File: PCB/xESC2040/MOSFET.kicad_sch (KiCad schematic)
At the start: 6 parts, among them J6 Conn_02x02_Counter_Clockwise, Q1 BSC026N08NS5, Q2 BSC026N08NS5

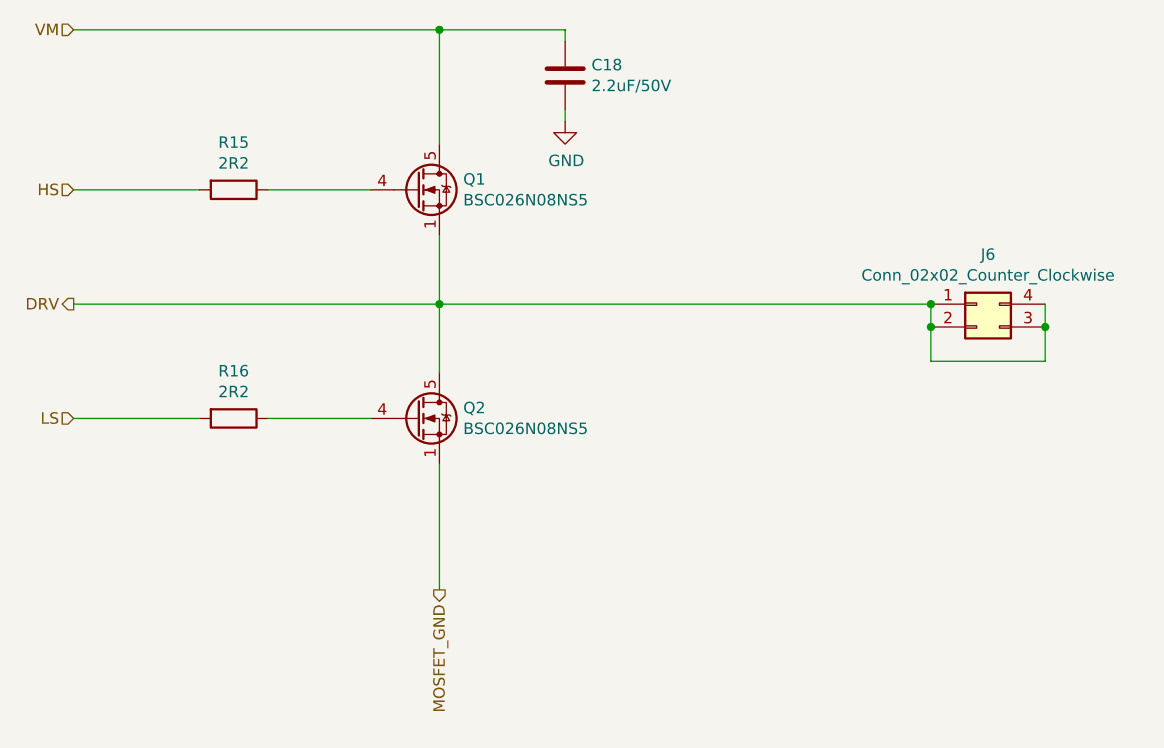
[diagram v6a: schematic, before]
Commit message: updated wrong BOM part number
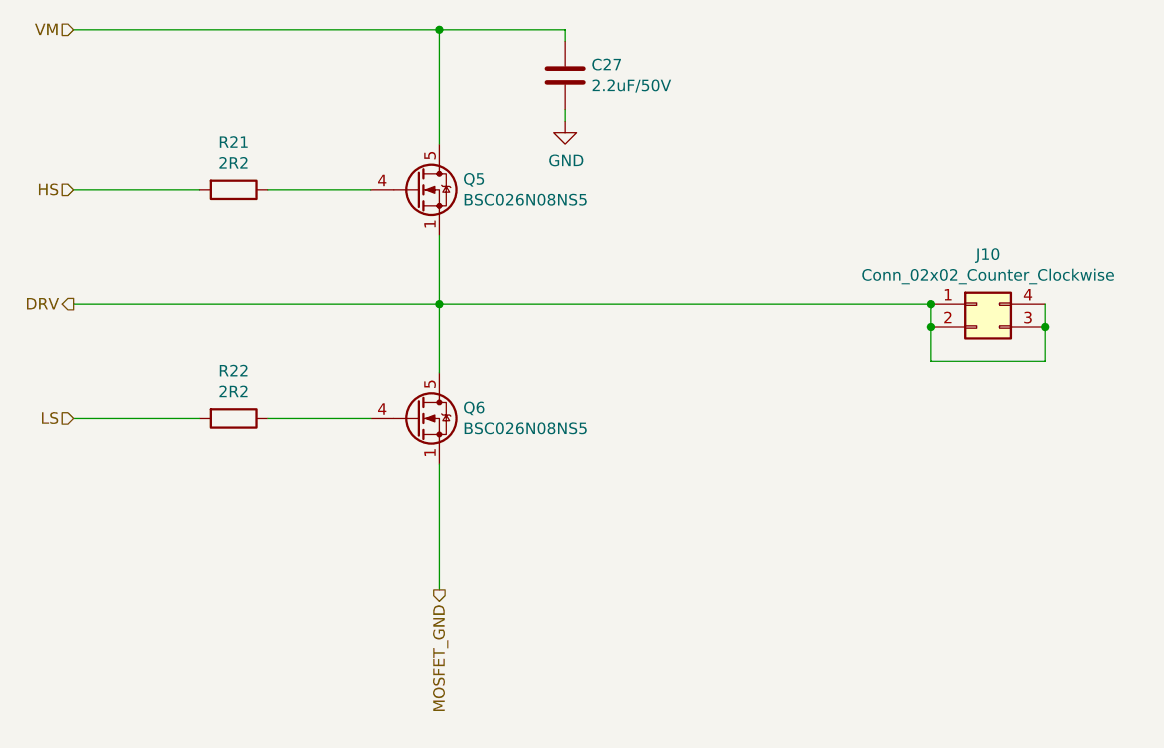
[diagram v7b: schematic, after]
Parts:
- renumbered C18 to C27, J6 to J10, Q1 to Q5, Q2 to Q6, R15 to R21, R16 to R22
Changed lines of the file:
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@@
     (effects (font (size 1.27 1.27)) (justify right))
   )
-  (symbol (lib_id "Transistor_FET:BSC026N08NS5") (at 173.99 71.12 0) (unit 1)
+  (symbol (lib_id "Transistor_FET:BSC026N08NS5") (at 173.99 71.12 0)
     (in_bom yes) (on_board yes)
-    (property "Reference" "Q1" (id 0) (at 179.1716 69.9516 0)
+    (property "Reference" "Q5" (id 0) (at 179.1716 69.9516 0)
       (effects (font (size 1.27 1.27)) (justify left))
     )
@@
     (pin "5")
   )
-  (symbol (lib_id "Transistor_FET:BSC026N08NS5") (at 173.99 96.52 0) (unit 1)
+  (symbol (lib_id "Transistor_FET:BSC026N08NS5") (at 173.99 96.52 0)
     (in_bom yes) (on_board yes)
-    (property "Reference" "Q2" (id 0) (at 179.1716 95.3516 0)
+    (property "Reference" "Q6" (id 0) (at 179.1716 95.3516 0)
       (effects (font (size 1.27 1.27)) (justify left))
     )
@@
     (pin "5")
   )
-  (symbol (lib_id "Device:R") (at 153.67 71.12 270) (unit 1)
+  (symbol (lib_id "Device:R") (at 153.67 71.12 270)
     (in_bom yes) (on_board yes)
-    (property "Reference" "R15" (id 0) (at 153.67 65.8622 90))
+    (property "Reference" "R21" (id 0) (at 153.67 65.8622 90))
     (property "Value" "2R2" (id 1) (at 153.67 68.1736 90))
     (property "Footprint" "Resistor_SMD:R_0603_1608Metric" (id 2) (at 153.67 69.342 90)
@@
     (pin "2")
   )
-  (symbol (lib_id "Device:R") (at 153.67 96.52 270) (unit 1)
+  (symbol (lib_id "Device:R") (at 153.67 96.52 270)
     (in_bom yes) (on_board yes)
-    (property "Reference" "R16" (id 0) (at 153.67 91.2622 90))
+    (property "Reference" "R22" (id 0) (at 153.67 91.2622 90))
     (property "Value" "2R2" (id 1) (at 153.67 93.5736 90))
     (property "Footprint" "Resistor_SMD:R_0603_1608Metric" (id 2) (at 153.67 94.742 90)
@@
     (pin "2")
   )
-  (symbol (lib_id "Device:C") (at 190.5 58.42 0) (unit 1)
+  (symbol (lib_id "Device:C") (at 190.5 58.42 0)
     (in_bom yes) (on_board yes)
-    (property "Reference" "C18" (id 0) (at 193.421 57.2516 0)
+    (property "Reference" "C27" (id 0) (at 193.421 57.2516 0)
       (effects (font (size 1.27 1.27)) (justify left))
     )
@@
     (pin "2")
   )
-  (symbol (lib_id "power:GND") (at 190.5 63.5 0) (unit 1)
+  (symbol (lib_id "power:GND") (at 190.5 63.5 0)
     (in_bom yes) (on_board yes)
-    (property "Reference" "#PWR022" (id 0) (at 190.5 69.85 0)
+    (property "Reference" "#PWR037" (id 0) (at 190.5 69.85 0)
       (effects (font (size 1.27 1.27)) hide)
     )
@@
     (pin "1")
   )
-  (symbol (lib_id "Connector_Generic:Conn_02x02_Counter_Clockwise") (at 236.22 83.82 0) (unit 1)
+  (symbol (lib_id "Connector_Generic:Conn_02x02_Counter_Clockwise") (at 236.22 83.82 0)
     (in_bom yes) (on_board yes)
-    (property "Reference" "J6" (id 0) (at 237.49 78.3082 0))
+    (property "Reference" "J10" (id 0) (at 237.49 78.3082 0))
     (property "Value" "Conn_02x02_Counter_Clockwise" (id 1) (at 237.49 80.6196 0))
     (property "Footprint" "Connector_PinHeader_2.54mm:PinHeader_2x02_P2.54mm_Vertical" (id 2) (at 236.22 83.82 0)
